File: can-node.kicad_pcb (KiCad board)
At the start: 2 copper layers, 68.6 x 69.1 mm, 38 parts, among them J1 Conn_01x02_Pin, J10 Conn_01x06_Pin, J13 SDA, J14 SCL, J15 Conn_01x03_Pin, J16 Conn_01x02_Pin, J17 Conn_01x02_Pin, J2 Conn_01x02_Pin, J3 RJ45, J4 RJ45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

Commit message: 3D-ified
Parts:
- moved J4 14.9 mm to (92.2, 93.0), turned to -90 degrees
- moved R13 1.02 mm to (99.8, 101.1)
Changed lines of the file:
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@@
   )
   (footprint "Resistor_THT:R_Axial_DIN0204_L3.6mm_D1.6mm_P5.08mm_Horizontal" (layer "F.Cu")
-    (at 98.806 101.092 90)
+    (at 99.822 101.092 90)
     (descr "Resistor, Axial_DIN0204 series, Axial, Horizontal, pin pitch=5.08mm, 0.167W, length*diameter=3.6*1.6mm^2, http://cdn-reichelt.de/documents/datenblatt/B400/1_4W%23YAG.pdf")
     (tags "Resistor Axial_DIN0204 series Axial Horizontal pin pitch 5.08mm 0.167W length 3.6mm diameter 1.6mm")
@@
       )
     )
+    (model "D:/anujv/Documents/KiCad/7.0/3dmodels/myesp.wrl" hide
+      (offset (xyz 0 0 0))
+      (scale (xyz 1 1 1))
+      (rotate (xyz 0 0 0))
+    )
+    (model "D:/anujv/Documents/KiCad/7.0/3dmodels/esp32 with header v2.obj" hide
+      (offset (xyz 0 0 0))
+      (scale (xyz 1 1 1))
+      (rotate (xyz 0 0 0))
+    )
+    (model "D:/anujv/Documents/KiCad/7.0/3dmodels/esp32 with header v2.step"
+      (offset (xyz -64.25 -150.5 7.5))
+      (scale (xyz 1 1 1))
+      (rotate (xyz 0 0 0))
+    )
+    (model "D:/anujv/Documents/KiCad/7.0/3dmodels/esp32 with header v2.stl" hide
+      (offset (xyz 0 0 0))
+      (scale (xyz 1 1 1))
+      (rotate (xyz 0 0 0))
+    )
   )
   (footprint "Resistor_THT:R_Axial_DIN0204_L3.6mm_D1.6mm_P5.08mm_Horizontal" (layer "F.Cu")
@@
     (pad "8" thru_hole circle (at 8.89 -2.54 90) (size 1.5 1.5) (drill 0.76) (layers "*.Cu" "*.Mask")
       (net 15 "CAN-") (pintype "passive"))
-    (model "${KICAD6_3DMODEL_DIR}/Connector_RJ.3dshapes/RJ45_Amphenol_54602-x08_Horizontal.wrl"
-      (offset (xyz 0 0 0))
+    (model "${KICAD6_3DMODEL_DIR}/Connector_RJ.3dshapes/RJ45_Amphenol_54602-x08_Horizontal.wrl" hide
+      (offset (xyz 0 0 0))
+      (scale (xyz 1 1 1))
+      (rotate (xyz 0 0 0))
+    )
+    (model "D:/anujv/Documents/KiCad/7.0/3dmodels/RJ45_SS_6488_FLS_Stewart.step"
+      (offset (xyz 4.5 -6.5 0))
       (scale (xyz 1 1 1))
       (rotate (xyz 0 0 0))
@@
     (pad "4" smd rect (at 7.62 4.572 270) (size 2.032 2.032) (layers "F.Cu" "F.Paste" "F.Mask")
       (net 2 "GND") (pinfunction "GND") (pintype "passive") (thermal_bridge_angle 45))
+    (model "D:/anujv/Documents/KiCad/7.0/3dmodels/MIni - 360.step"
+      (offset (xyz 0 0.75 -16))
+      (scale (xyz 1 1 1))
+      (rotate (xyz 0 0 -90))
+    )
   )
   (footprint "Resistor_THT:R_Axial_DIN0204_L3.6mm_D1.6mm_P5.08mm_Horizontal" (layer "F.Cu")
@@
       (scale (xyz 1 1 1))
       (rotate (xyz 0 0 0))
+    )
+    (model "D:/anujv/Documents/KiCad/7.0/3dmodels/MD13S.STEP"
+      (offset (xyz -2.5 -25 15))
+      (scale (xyz 1 1 1))
+      (rotate (xyz -90 0 90))
     )
   )
@@
       (rotate (xyz 0 0 0))
     )
+    (model "D:/anujv/Documents/KiCad/7.0/3dmodels/MPU-9250.stp"
+      (offset (xyz 1 1 11))
+      (scale (xyz 0.8 0.8 0.8))
+      (rotate (xyz -90 0 0))
+    )
   )
   (footprint "Connector_Wire:SolderWire-0.1sqmm_1x01_D0.4mm_OD1mm" (layer "F.Cu")
@@
   )
   (footprint "Connector_RJ:RJ45_Amphenol_54602-x08_Horizontal" (layer "F.Cu")
-    (at 80.498 102.108 90)
+    (at 92.202 92.964 -90)
     (descr "8 Pol Shallow Latch Connector, Modjack, RJ45 (https://cdn.amphenol-icc.com/media/wysiwyg/files/drawing/c-bmj-0102.pdf)")
     (tags "RJ45")
@@
     (property "ki_keywords" "8P8C RJ socket connector")
     (attr through_hole)
-    (fp_text reference "J4" (at 4.445 -5 90) (layer "F.SilkS")
+    (fp_text reference "J4" (at -5.334 -0.508 -180) (layer "F.SilkS")
         (effects (font (size 1 1) (thickness 0.15)))
     )
@@
     (fp_line (start 12.095 13.97) (end -3.205 13.97)
       (stroke (width 0.12) (type solid)) (layer "F.Fab"))
-    (pad "" np_thru_hole circle (at -1.27 6.35 90) (size 3.2 3.2) (drill 3.2) (layers "*.Cu" "*.Mask"))
-    (pad "" np_thru_hole circle (at 10.16 6.35 90) (size 3.2 3.2) (drill 3.2) (layers "*.Cu" "*.Mask"))
-    (pad "1" thru_hole rect (at 0 0 90) (size 1.5 1.5) (drill 0.76) (layers "*.Cu" "*.Mask")
+    (pad "" np_thru_hole circle (at -1.27 6.35 270) (size 3.2 3.2) (drill 3.2) (layers "*.Cu" "*.Mask"))
+    (pad "" np_thru_hole circle (at 10.16 6.35 270) (size 3.2 3.2) (drill 3.2) (layers "*.Cu" "*.Mask"))
+    (pad "1" thru_hole rect (at 0 0 270) (size 1.5 1.5) (drill 0.76) (layers "*.Cu" "*.Mask")
       (net 2 "GND") (pintype "passive"))
-    (pad "2" thru_hole circle (at 1.27 -2.54 90) (size 1.5 1.5) (drill 0.76) (layers "*.Cu" "*.Mask")
+    (pad "2" thru_hole circle (at 1.27 -2.54 270) (size 1.5 1.5) (drill 0.76) (layers "*.Cu" "*.Mask")
       (net 2 "GND") (pintype "passive"))
-    (pad "3" thru_hole circle (at 2.54 0 90) (size 1.5 1.5) (drill 0.76) (layers "*.Cu" "*.Mask")
+    (pad "3" thru_hole circle (at 2.54 0 270) (size 1.5 1.5) (drill 0.76) (layers "*.Cu" "*.Mask")
       (net 16 "unconnected-(J4-Pad3)") (pintype "passive+no_connect"))
-    (pad "4" thru_hole circle (at 3.81 -2.54 90) (size 1.5 1.5) (drill 0.76) (layers "*.Cu" "*.Mask")
+    (pad "4" thru_hole circle (at 3.81 -2.54 270) (size 1.5 1.5) (drill 0.76) (layers "*.Cu" "*.Mask")
       (net 17 "unconnected-(J4-Pad4)") (pintype "passive+no_connect"))
-    (pad "5" thru_hole circle (at 5.08 0 90) (size 1.5 1.5) (drill 0.76) (layers "*.Cu" "*.Mask")
+    (pad "5" thru_hole circle (at 5.08 0 270) (size 1.5 1.5) (drill 0.76) (layers "*.Cu" "*.Mask")
       (net 18 "unconnected-(J4-Pad5)") (pintype "passive+no_connect"))
-    (pad "6" thru_hole circle (at 6.35 -2.54 90) (size 1.5 1.5) (drill 0.76) (layers "*.Cu" "*.Mask")
+    (pad "6" thru_hole circle (at 6.35 -2.54 270) (size 1.5 1.5) (drill 0.76) (layers "*.Cu" "*.Mask")
       (net 19 "unconnected-(J4-Pad6)") (pintype "passive+no_connect"))
-    (pad "7" thru_hole circle (at 7.62 0 90) (size 1.5 1.5) (drill 0.76) (layers "*.Cu" "*.Mask")
+    (pad "7" thru_hole circle (at 7.62 0 270) (size 1.5 1.5) (drill 0.76) (layers "*.Cu" "*.Mask")
       (net 14 "CAN+") (pintype "passive"))
-    (pad "8" thru_hole circle (at 8.89 -2.54 90) (size 1.5 1.5) (drill 0.76) (layers "*.Cu" "*.Mask")
+    (pad "8" thru_hole circle (at 8.89 -2.54 270) (size 1.5 1.5) (drill 0.76) (layers "*.Cu" "*.Mask")
       (net 15 "CAN-") (pintype "passive"))
-    (model "${KICAD6_3DMODEL_DIR}/Connector_RJ.3dshapes/RJ45_Amphenol_54602-x08_Horizontal.wrl"
-      (offset (xyz 0 0 0))
-      (scale (xyz 1 1 1))
-      (rotate (xyz 0 0 0))
+    (model "${KICAD6_3DMODEL_DIR}/Connector_RJ.3dshapes/RJ45_Amphenol_54602-x08_Horizontal.wrl" hide
+      (offset (xyz 0 0 0))
+      (scale (xyz 1 1 1))
+      (rotate (xyz 0 0 0))
+    )
+    (model "D:/anujv/Documents/KiCad/7.0/3dmodels/RJ45_SS_6488_FLS_Stewart.step"
+      (offset (xyz 4.5 -6.5 0))
+      (scale (xyz 1 1 1))
+      (rotate (xyz 0 0 0))

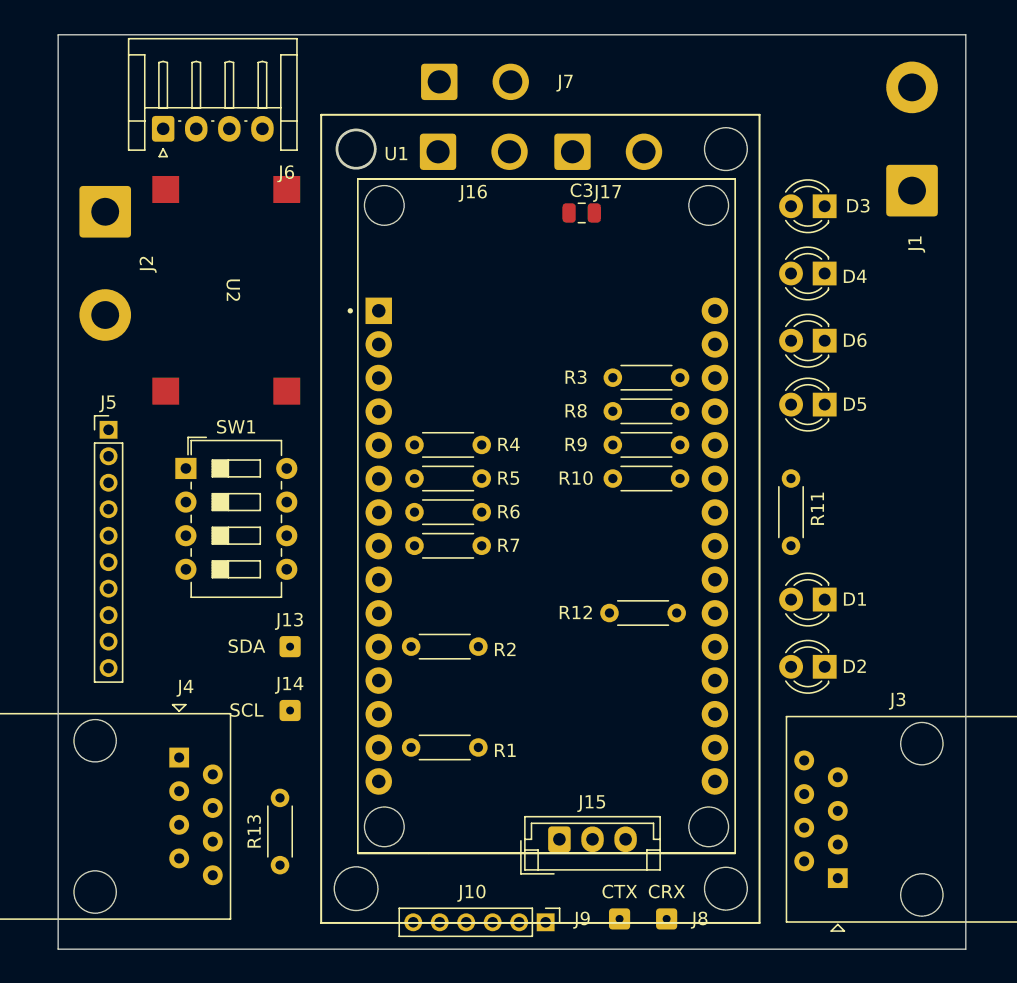
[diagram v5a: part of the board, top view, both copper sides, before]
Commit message: fixed footprints
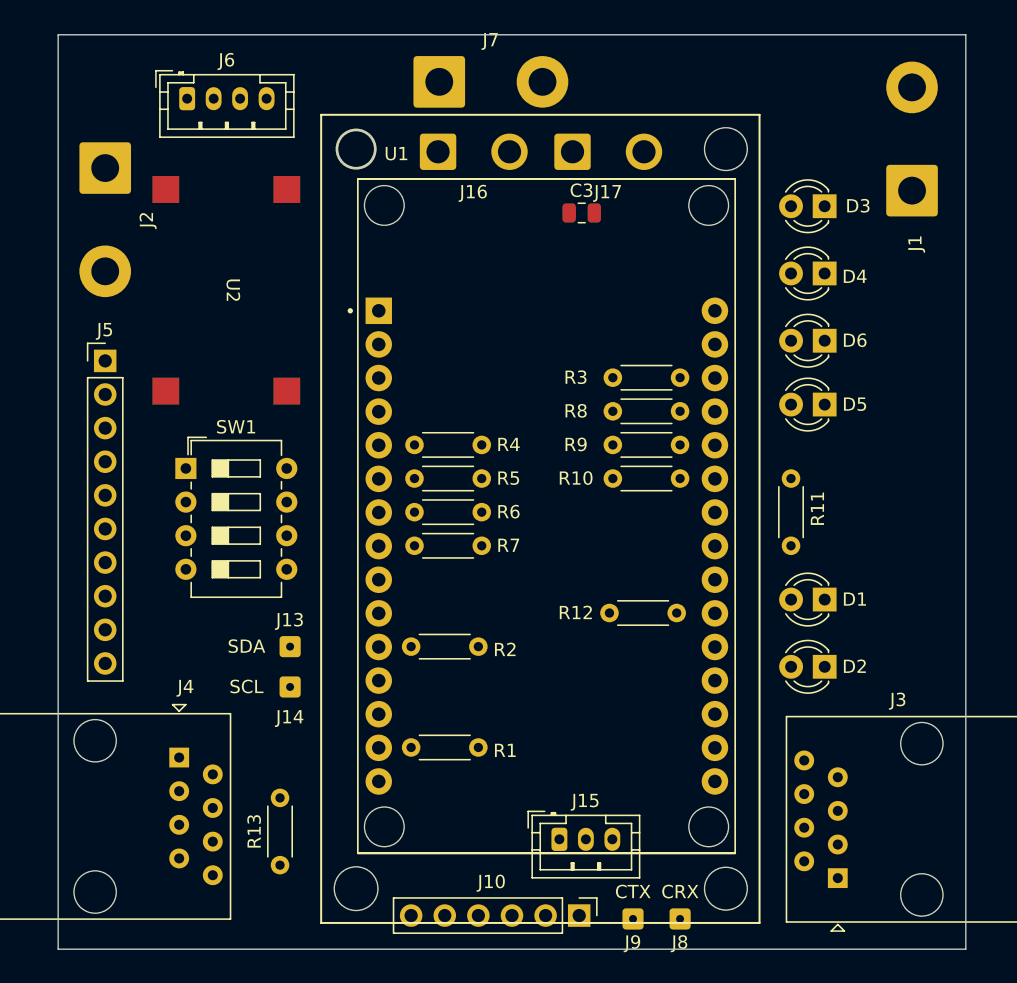
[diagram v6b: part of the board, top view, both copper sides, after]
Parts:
- J10: footprint Connector_PinHeader_2.00mm:PinHeader_1x06_P2.00mm_Vertical -> Connector_PinHeader_2.54mm:PinHeader_1x06_P2.54mm_Vertical
- J15: footprint Connector_JST:JST_EH_B3B-EH-A_1x03_P2.50mm_Vertical -> Connector_JST:JST_PH_B3B-PH-K_1x03_P2.00mm_Vertical
- J5: footprint Connector_PinHeader_2.00mm:PinHeader_1x10_P2.00mm_Vertical -> Connector_PinHeader_2.54mm:PinHeader_1x10_P2.54mm_Vertical
- J6: footprint Connector_JST:JST_EH_S4B-EH_1x04_P2.50mm_Horizontal -> Connector_JST:JST_PH_B4B-PH-K_1x04_P2.00mm_Vertical
- J7: footprint Connector_Wire:SolderWire-1sqmm_1x02_P5.4mm_D1.4mm_OD2.7mm -> Connector_Wire:SolderWire-1.5sqmm_1x02_P7.8mm_D1.7mm_OD3.9mm
- moved J5 5.21 mm to (86.6, 63.0)
- moved J2 3.30 mm to (86.6, 48.4)
- moved J6 2.91 mm to (92.8, 43.2)
- moved J10 2.59 mm to (122.4, 104.9)
- moved J14 1.78 mm to (100.6, 87.6)
- moved J9 1.02 mm to (126.5, 105.2)
- moved J8 1.02 mm to (130.0, 105.2)

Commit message: routing attempt
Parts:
- moved C3 11.2 mm to (130.1, 60.2), turned to -90 degrees
- moved D3 11.0 mm to (147.8, 59.9)
- moved D4 10.8 mm to (147.8, 64.8)
- moved D5 10.6 mm to (147.8, 74.4)
- moved D6 10.6 mm to (147.8, 69.6)
- moved R3 7.62 mm to (124.7, 71.9)
- moved D2 7.15 mm to (147.8, 84.1)
- moved D1 7.08 mm to (147.8, 79.2)
- moved R11 6.14 mm to (137.7, 70.9)
- moved R10 5.09 mm to (124.7, 66.8)
- moved R9 5.09 mm to (124.7, 64.3)
- moved R12 4.57 mm to (125.2, 82.0), turned to 0 degrees
- moved R13 3.06 mm to (100.1, 104.1)
- moved R8 2.55 mm to (124.7, 69.3)
- moved J8 0.57 mm to (129.8, 104.6)
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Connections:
- R10 pad 2: LED3 -> LED1
- R3 pad 2: LED0 -> LED3
- R8 pad 2: LED1 -> LED2
- R9 pad 2: LED2 -> LED0
- U1 pad 10: FSYNC -> INT
- U1 pad 19: ENC-B -> ENC-A
- U1 pad 22: ENC-A -> ENC-B
- U1 pad 23: PWM -> DIR
- U1 pad 24: DIR -> PWM
- U1 pad 9: INT -> FSYNC
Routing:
- net +5V: track 0.00 -> 97.2 mm, vias 0 -> 2
- net +3.3V: track 0.00 -> 84.5 mm
- net CAN+: track 0.00 -> 76.2 mm
- net +12 V: track 0.00 -> 68.5 mm
- net CAN-Rx: track 0.00 -> 64.7 mm
- net ENC-A: track 0.00 -> 63.2 mm
- net CAN-: track 0.00 -> 62.0 mm
- net CAN-Tx: track 0.00 -> 60.5 mm
- net ENC-B: track 0.00 -> 55.4 mm
- net Net-(D3-A): track 0.00 -> 44.6 mm
- net Net-(D2-A): track 0.00 -> 41.4 mm
- net Net-(D4-A): track 0.00 -> 40.2 mm
- net Net-(D6-A): track 0.00 -> 38.6 mm
- net Net-(D5-A): track 0.00 -> 36.6 mm
- net FSYNC: track 0.00 -> 36.6 mm
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- added copper zone on B.Cu, net GND
- added copper zone on F.Cu, net GND

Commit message: update for 3D
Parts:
- removed R13: 60, Resistor_THT:R_Axial_DIN0204_L3.6mm_D1.6mm_P5.08mm_Horizontal
- added J11: Conn_01x02_Socket, Connector_Wire:SolderWire-0.1sqmm_1x02_P3.6mm_D0.4mm_OD1mm, F.Cu at (100.1, 102.7)
- D1: value LED -> STATUS
- D2: value LED -> POWER
- J15: footprint Connector_JST:JST_PH_B3B-PH-K_1x03_P2.00mm_Vertical -> Connector_JST:JST_PH_S3B-PH-K_1x03_P2.00mm_Horizontal
- moved J15 6.19 mm to (122.7, 93.2)
- moved J16 0.19 mm to (111.8, 47.4)
- moved J17 0.19 mm to (121.9, 47.4)
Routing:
- net +12 V: track 68.5 -> 90.8 mm
- net MOTOR_A: track 6.32 -> 12.8 mm
- net MOTOR_B: track 5.32 -> 10.8 mm
- net PWM: track 33.5 -> 28.3 mm
- net DIR: track 29.9 -> 24.8 mm
- net GND: vias 0 -> 12
- net (no net): vias 0 -> 4
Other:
- outline, holes or cut-outs redrawn
